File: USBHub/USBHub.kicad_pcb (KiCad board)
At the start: 4 copper layers, 55.9 x 52.1 mm, 96 parts, among them J1 PJ-102, J2 10033526-N3212MLF, J3 73725-0110RLF, J4 73725-0110RLF, J5 73725-0110RLF, J6 73725-0110RLF, J7 73725-0110RLF, J8 73725-0110RLF, J9 73725-0110RLF, U1 74LVC1G08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

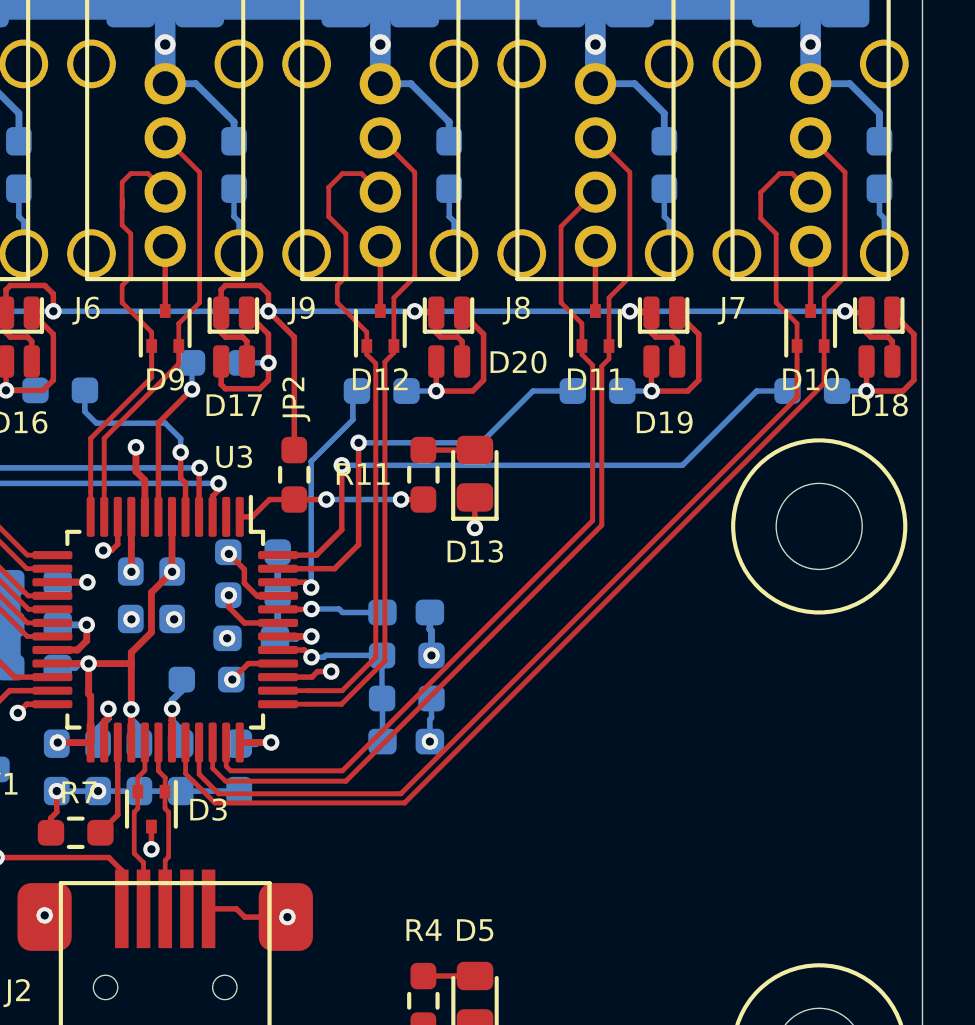
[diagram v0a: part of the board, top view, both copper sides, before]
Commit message: Update to USB hub.
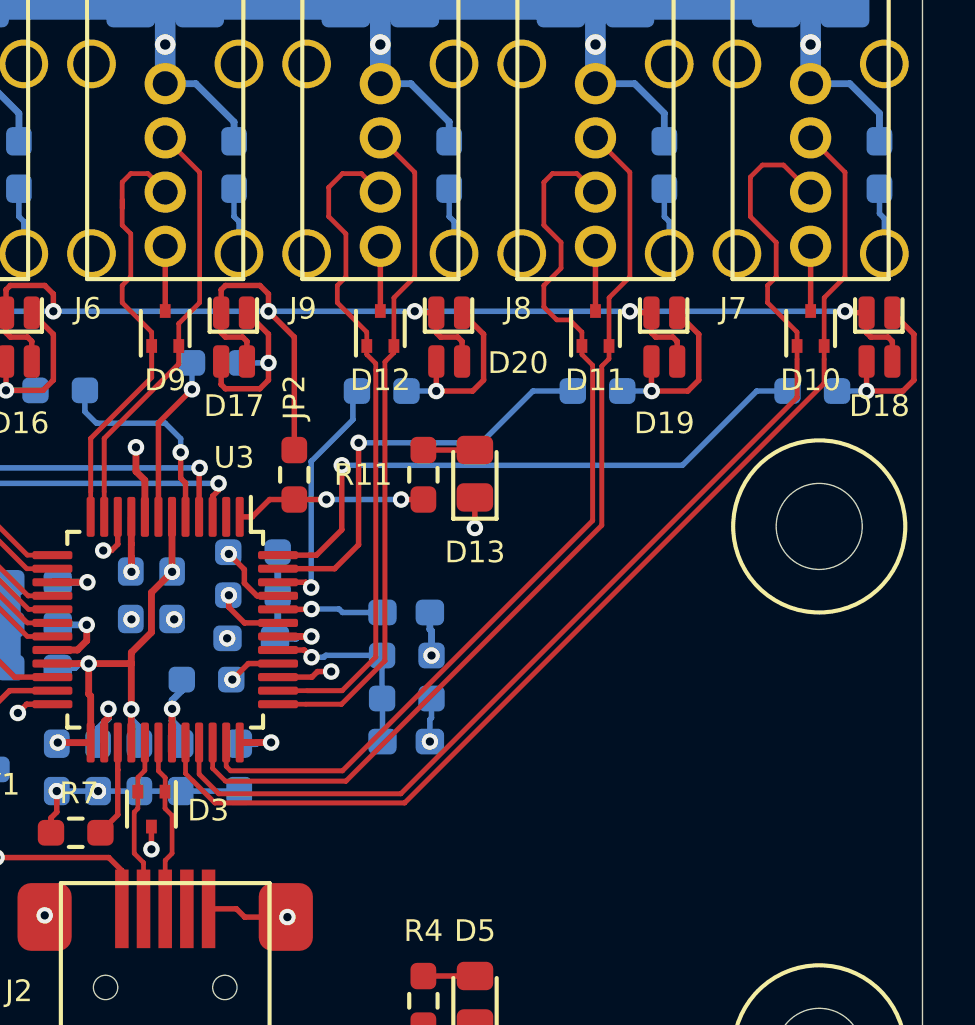
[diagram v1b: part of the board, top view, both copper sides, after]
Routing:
- net /U6D+: track 31.4 -> 34.6 mm
- net /U5D+: track 40.2 -> 41.6 mm
